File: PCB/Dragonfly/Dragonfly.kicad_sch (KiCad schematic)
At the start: 0 parts

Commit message: hell yeah
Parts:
- added U1: STM32F405RGTx, Package_QFP:LQFP-64_10x10mm_P0.5mm, symbol MCU_ST_STM32F4:STM32F405RGTx
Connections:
- new net: U1.18 (VSS), U1.63 (VSS)
- new net PA0: U1.14 (PA0)
- new net PA1: U1.15 (PA1)
- new net PA10: U1.43 (PA10)
- new net PA11: U1.44 (PA11)
- new net PA12: U1.45 (PA12)
- new net PA13: U1.46 (PA13)
- new net PA14: U1.49 (PA14)
- new net PA15: U1.50 (PA15)
- new net PA2: U1.16 (PA2)
- new net PA3: U1.17 (PA3)
- new net PA4: U1.20 (PA4)
- new net PA5: U1.21 (PA5)
- new net PA6: U1.22 (PA6)
- new net PA7: U1.23 (PA7)
- new net PA8: U1.41 (PA8)
- new net PA9: U1.42 (PA9)
- new net PB0: U1.26 (PB0)
- new net PB1: U1.27 (PB1)
- new net PB10: U1.29 (PB10)
- new net PB11: U1.30 (PB11)
- new net PB12: U1.33 (PB12)
- new net PB13: U1.34 (PB13)
- new net PB14: U1.35 (PB14)
- new net PB15: U1.36 (PB15)
- new net PB2: U1.28 (PB2)
- new net PB3: U1.55 (PB3)
- new net PB4: U1.56 (PB4)
- new net PB5: U1.57 (PB5)
- new net PB6: U1.58 (PB6)
- new net PB7: U1.59 (PB7)
- new net PB8: U1.61 (PB8)
- new net PB9: U1.62 (PB9)
- new net PC0: U1.8 (PC0)
- new net PC1: U1.9 (PC1)
- new net PC10: U1.51 (PC10)
- new net PC11: U1.52 (PC11)
- new net PC12: U1.53 (PC12)
- new net PC13: U1.2 (PC13)
- new net PC14: U1.3 (PC14)
- new net PC15: U1.4 (PC15)
- new net PC2: U1.10 (PC2)
- new net PC3: U1.11 (PC3)
- new net PC4: U1.24 (PC4)
- new net PC5: U1.25 (PC5)
- new net PC6: U1.37 (PC6)
- new net PC8: U1.38 (PC7)
- new net PC9: U1.39 (PC8)

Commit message: updated
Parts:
- added +10ppm: 32.768 kHz, symbol Device:Crystal
- added C1, C2: 100pf, symbol Device:C
- added C3, C4: 12pf, symbol Device:C
- added SW1: SW_SPDT_312, symbol Switch:SW_SPDT_312
- added X1: TSX-3225, TSX-3225, symbol TSX-3225:TSX-3225
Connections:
- net PC9 is gone; now on net PC8: U1.39 (PC8)
- net PC8: no longer U1.38 (PC7)
- net CP9: now reaches U1.40 (PC9)
- net at U1.5 (PH0): now also C1.2, X1.1
- net PD2: now reaches U1.54 (PD2)
- net at U1.6 (PH1): now also C2.2, X1.3
- net BOOT0: now reaches U1.60 (BOOT0)
- net NRST: now reaches U1.7 (NRST)
- net PA14: no longer names the net of U1.49 (PA14)
- net PA14: now also +10ppm.2, C3.1
- net PA15: no longer names the net of U1.50 (PA15)
- net PA15: now also +10ppm.1, C4.1
- new net: C2.1, X1.4
- new net: C1.1, X1.2
- new net GND: C3.2, C4.2
- new net PC7: U1.38 (PC7)
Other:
- note added: "MIAN MCU"
- moved on the sheet: U1

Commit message: updates
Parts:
- removed SW1: SW_SPDT_312, symbol Switch:SW_SPDT_312
- added C5: 100nf, symbol Device:C
- added R1: 10kΩ NC, symbol Device:R
- added R2, R3: 10kΩ, symbol Device:R
- added SW1, SW2: SW_SPST, symbol Switch:SW_SPST
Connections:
- net BOOT0: now also R2.2, SW2.1 (A)
- net GND: now also R2.1, R3.2
- net NRST: now also C5.1, R1.2, SW1.1 (A)
- net PB2: now also R3.1
- new net: C5.2, SW1.2 (B)
- new net VDD: R1.1, SW2.2 (B)
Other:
- note added: "BOOT Settings"
- note added: "Reset circuit"

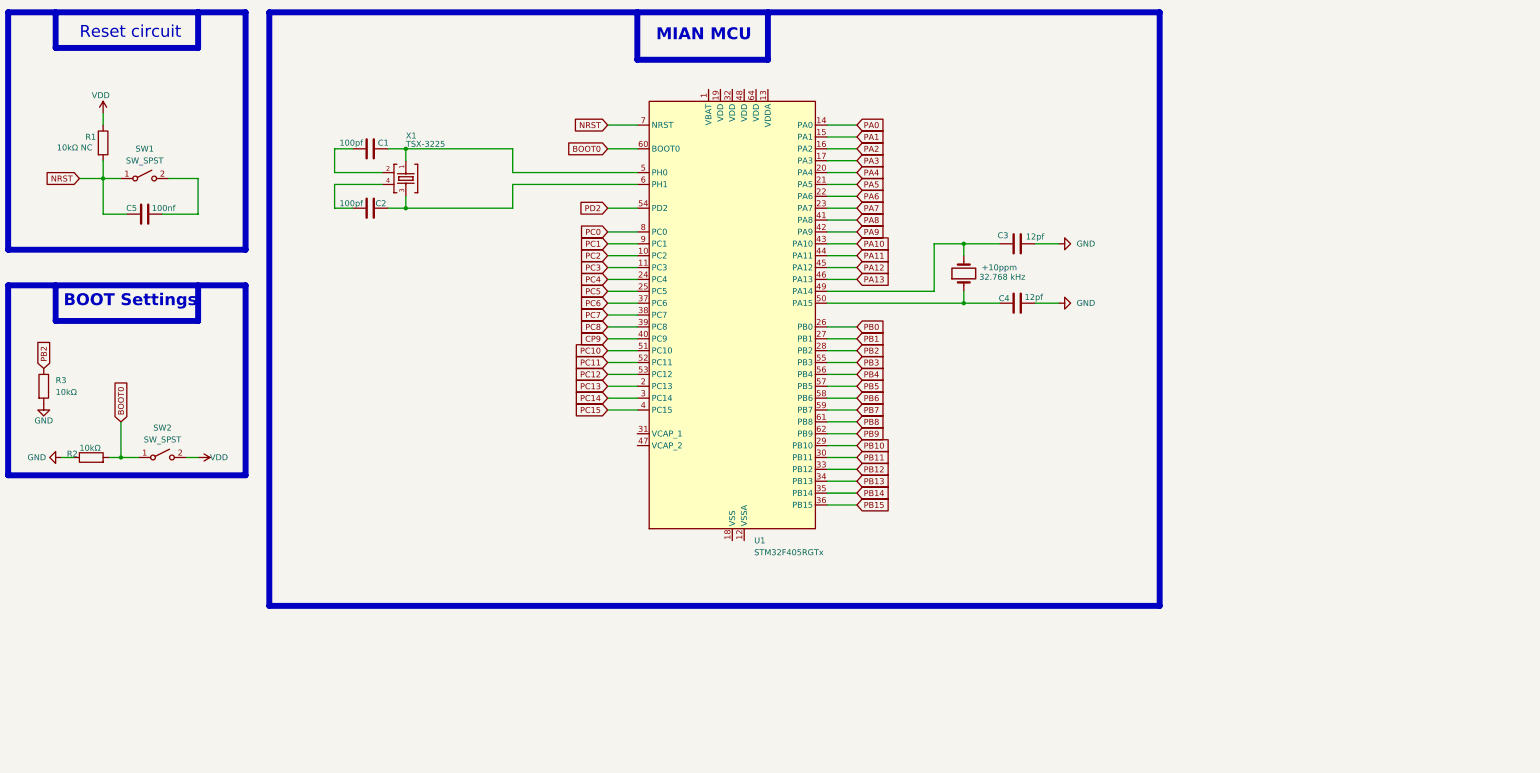
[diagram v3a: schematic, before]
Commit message: Update Dragonfly.kicad_sch
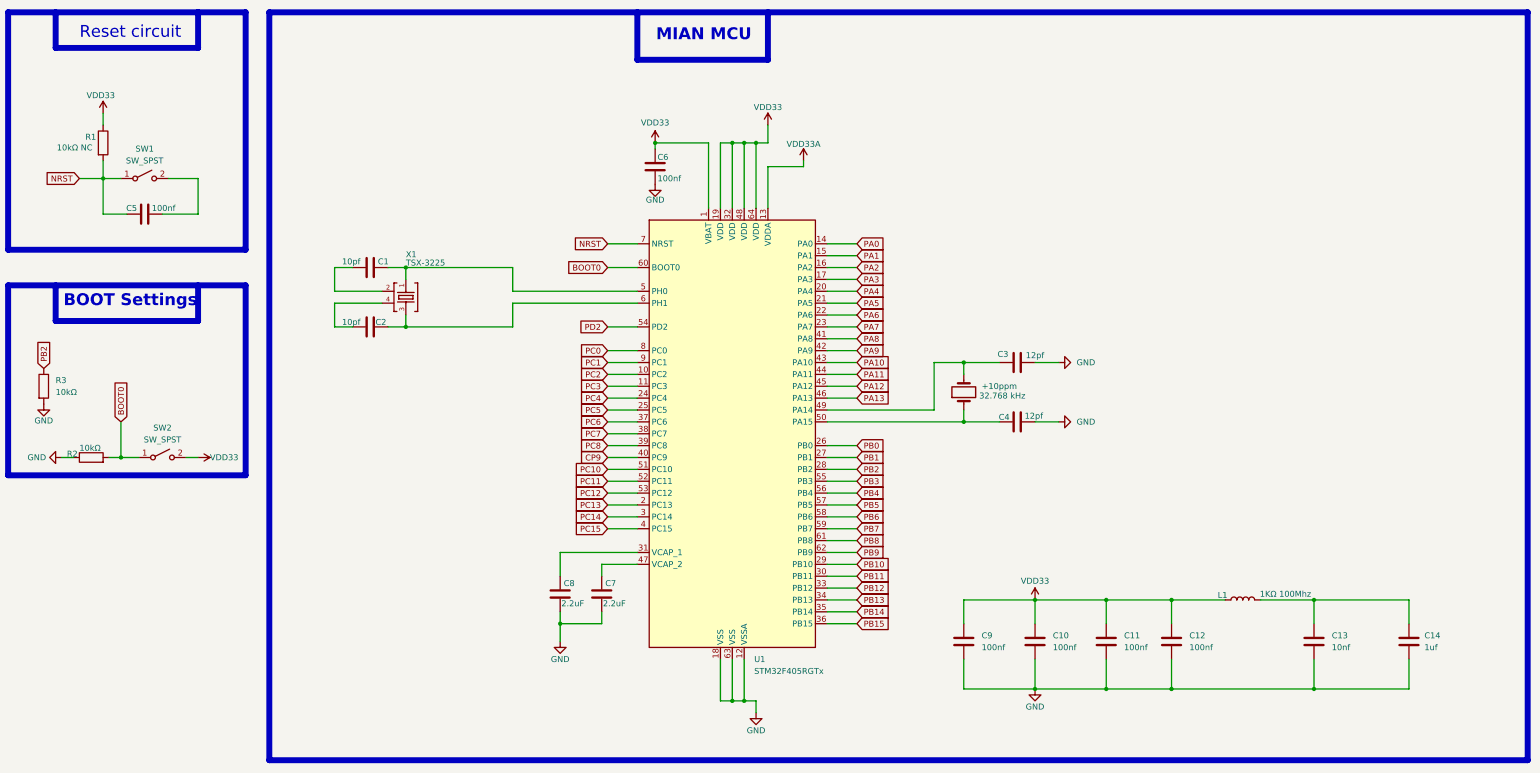
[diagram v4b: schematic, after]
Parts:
- added C10, C11, C12, C6, C9: 100nf, symbol Device:C
- added C13: 10nf, symbol Device:C
- added C14: 1uf, symbol Device:C
- added C7, C8: 2.2uF, symbol Device:C
- added L1: 1KΩ 100Mhz, symbol Device:L
- C1, C2: value 100pf -> 10pf
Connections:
- net VDD is gone; now on net VDD33: R1.1, SW2.2 (B)
- net GND: now also U1.12 (VSSA), U1.18 (VSS), U1.63 (VSS), C10.2, C11.2, C12.2, C13.2, C14.2, C6.2, C7.2, C8.2, C9.2
- net VDD33: now reaches U1.1 (VBAT)
- net VDD33: now also U1.19 (VDD), U1.32 (VDD), U1.48 (VDD), U1.64 (VDD), C10.1, C11.1, C12.1, C6.1, C9.1, L1.1
- net VDD33A: now reaches U1.13 (VDDA)
- net at U1.31 (VCAP_1): now also C8.1
- net at U1.47 (VCAP_2): now also C7.1
- new net: C13.1, C14.1, L1.2
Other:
- moved on the sheet: +10ppm, C1, C2, C3, C4, X1

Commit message: Update Dragonfly.kicad_sch
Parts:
- removed +10ppm: 32.768 kHz, symbol Device:Crystal
- added +10ppm1: 32.768 kHz, symbol Device:Crystal
- added C15, C19: 100nf, symbol Device:C
- added C16: 4.7uF, symbol Device:C
- added C17, C18: 10uf, symbol Device:C
- added D1: blue, symbol Device:D
- added D2: red, symbol Device:D
- added D3: DSK 34 SOD123, symbol Device:D
- added J1: Conn_01x04_Pin, symbol Connector:Conn_01x04_Pin
- added J2: Micro_SD_Card, symbol Connector:Micro_SD_Card
- added J3: USB_C_Receptacle_USB2.0_16P, symbol Connector:USB_C_Receptacle_USB2.0_16P
- added JP1: SolderJumper_2_Bridged, symbol Jumper:SolderJumper_2_Bridged
- added R4, R5, R7, R8: 5.1kΩ, symbol Device:R
- added R6: R, symbol Device:R
- added U2: (no value), Package_TO_SOT_SMD:SOT-89-3, symbol ME6231A33PG:ME6231A33PG
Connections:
- net PC14 is gone; now on an unnamed net: U1.3 (PC14)
- net PC15 is gone; now on an unnamed net: U1.4 (PC15)
- net CP9: now also J2.8 (DAT1)
- net GND: now also C15.2, C16.2, C17.2, C18.2, C19.2, D1.2 (A), D2.2 (A), J1.3 (Pin_3), J2.6 (VSS), J2.SH (SHIELD), J3.A1 (GND), J3.A12 (GND), J3.A8 (SBU1), J3.B1 (GND), J3.B12 (GND), J3.B8 (SBU2), J3.SH (SHIELD), R7.2, R8.2, U2.3 (VOUT)
- net PA11: now also J3.A6 (D+)
- net PA12: now also J3.B6 (D+)
- net PA13: now also J1.2 (Pin_2)
- net PB2: now also R4.1
- net PC10: now also J2.1 (DAT2)
- net PC11: now also J2.2 (DAT3/CD), R6.2
- net PC12: now also J2.5 (CLK)
- net PC8: now also J2.7 (DAT0)
- net PD2: now also J2.3 (CMD)
- net VDD33: now also C15.1, C16.1, C17.1, J1.1 (Pin_1), J2.4 (VDD), R5.1, R6.1, U2.1 (GND)
- net VDD33A: now also C13.1, C14.1, L1.2
- net at C4.1: now also +10ppm1.1; no longer U1.50 (PA15)
- net at C3.1: now also +10ppm1.2; no longer U1.49 (PA14)
- new net: D1.1 (K), R4.2
- new net: D2.1 (K), R5.2
- new net CC1: J3.A5 (CC1), R7.1
- new net CC2: J3.B5 (CC2), R8.1
- new net PA14: J1.4 (Pin_4), U1.49 (PA14)
- new net PA15: U1.50 (PA15)
- new net VBUS: C19.1, D3.1 (K), J3.A4 (VBUS), J3.A9 (VBUS), J3.B4 (VBUS), J3.B9 (VBUS), JP1.1 (A)
- new net VCC: C18.1, D3.2 (A), JP1.2 (B), U2.2 (VIN)
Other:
- note added: "Indicator light"
- note added: "SW debug download interface"
- note added: "TF interface"
- note added: "USB-C 16 PIN"
- note added: "VCC -> 3.3V Power conversion"

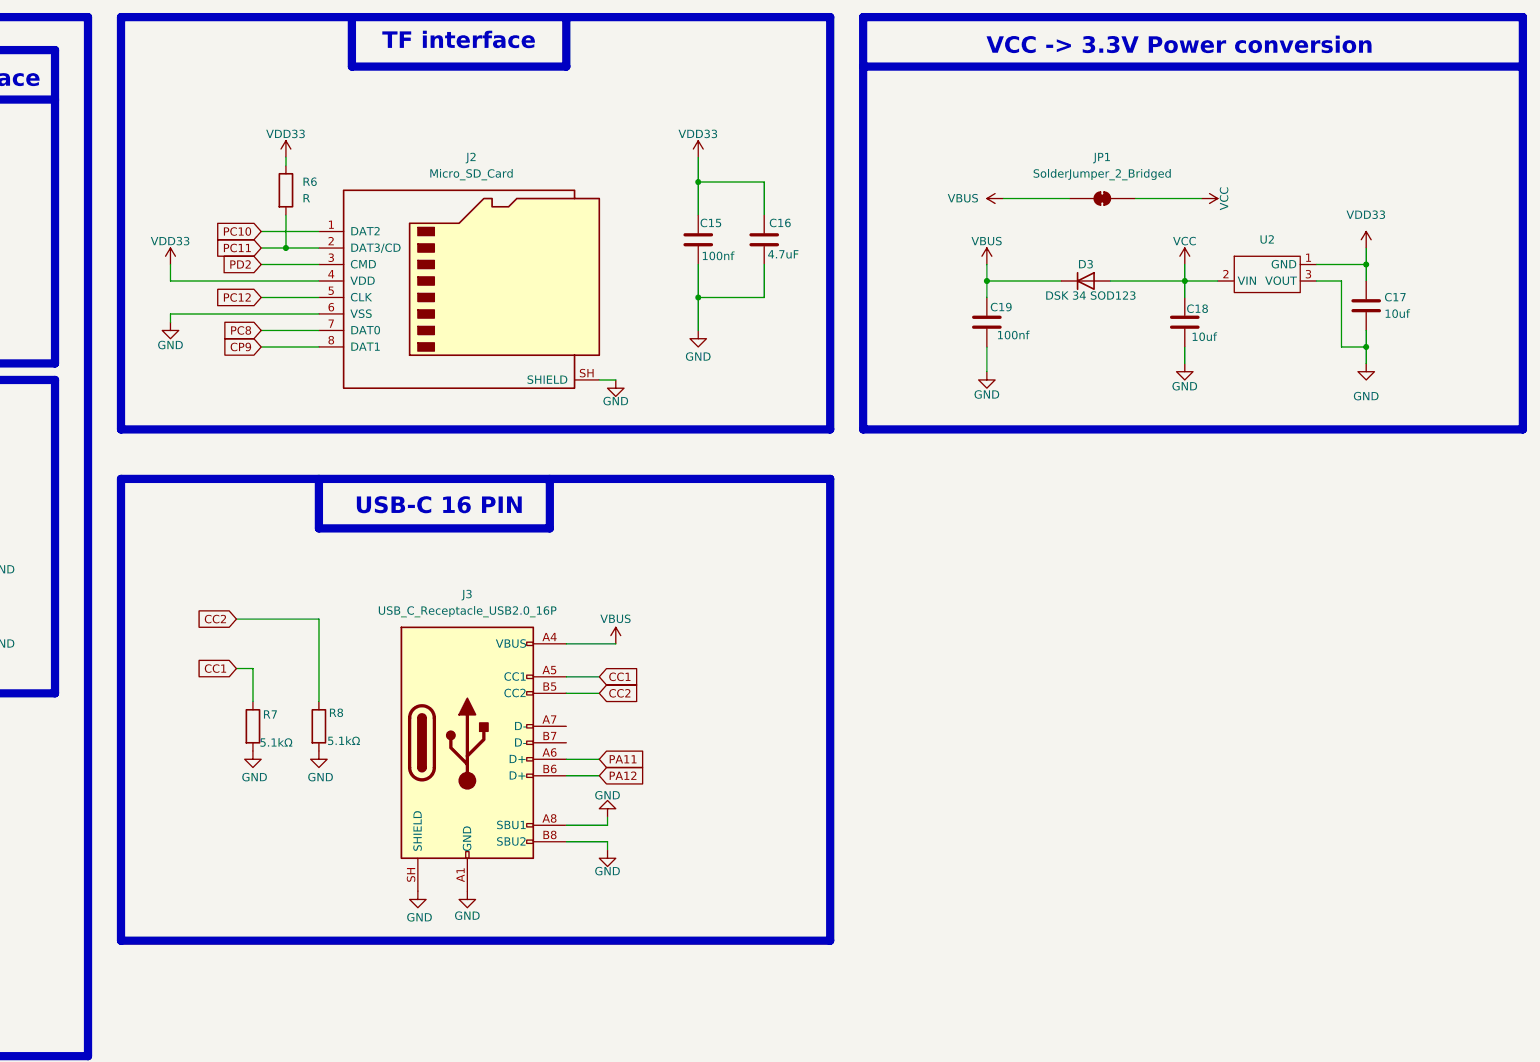
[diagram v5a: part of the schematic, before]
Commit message: Update Dragonfly.kicad_sch
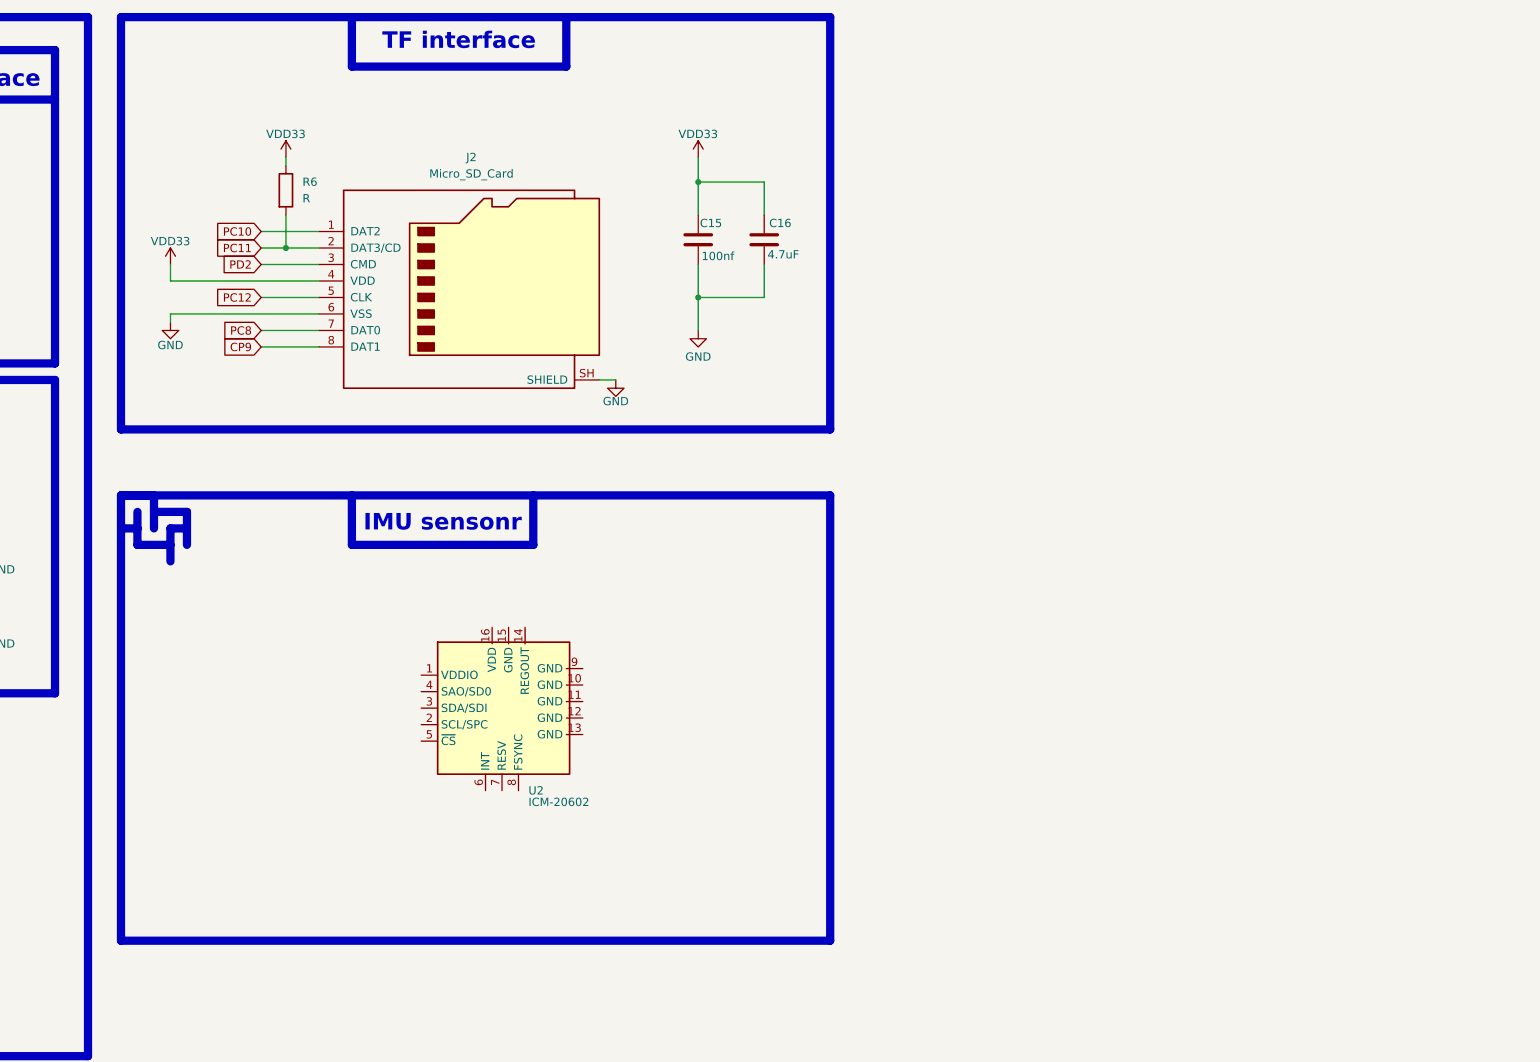
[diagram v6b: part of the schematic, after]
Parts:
- removed C17, C18: 10uf, symbol Device:C
- removed C19: 100nf, symbol Device:C
- removed D3: DSK 34 SOD123, symbol Device:D
- removed J3: USB_C_Receptacle_USB2.0_16P, symbol Connector:USB_C_Receptacle_USB2.0_16P
- removed JP1: SolderJumper_2_Bridged, symbol Jumper:SolderJumper_2_Bridged
- removed R7, R8: 5.1kΩ, symbol Device:R
- removed U2: (no value), Package_TO_SOT_SMD:SOT-89-3, symbol ME6231A33PG:ME6231A33PG
- added U2: ICM-20602, Package_LGA:LGA-16_3x3mm_P0.5mm_LayoutBorder3x5y, symbol Sensor_Motion:ICM-20602
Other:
- note added: "IMU sensonr"
- note removed: "USB-C 16 PIN"
- note removed: "VCC -> 3.3V Power conversion"

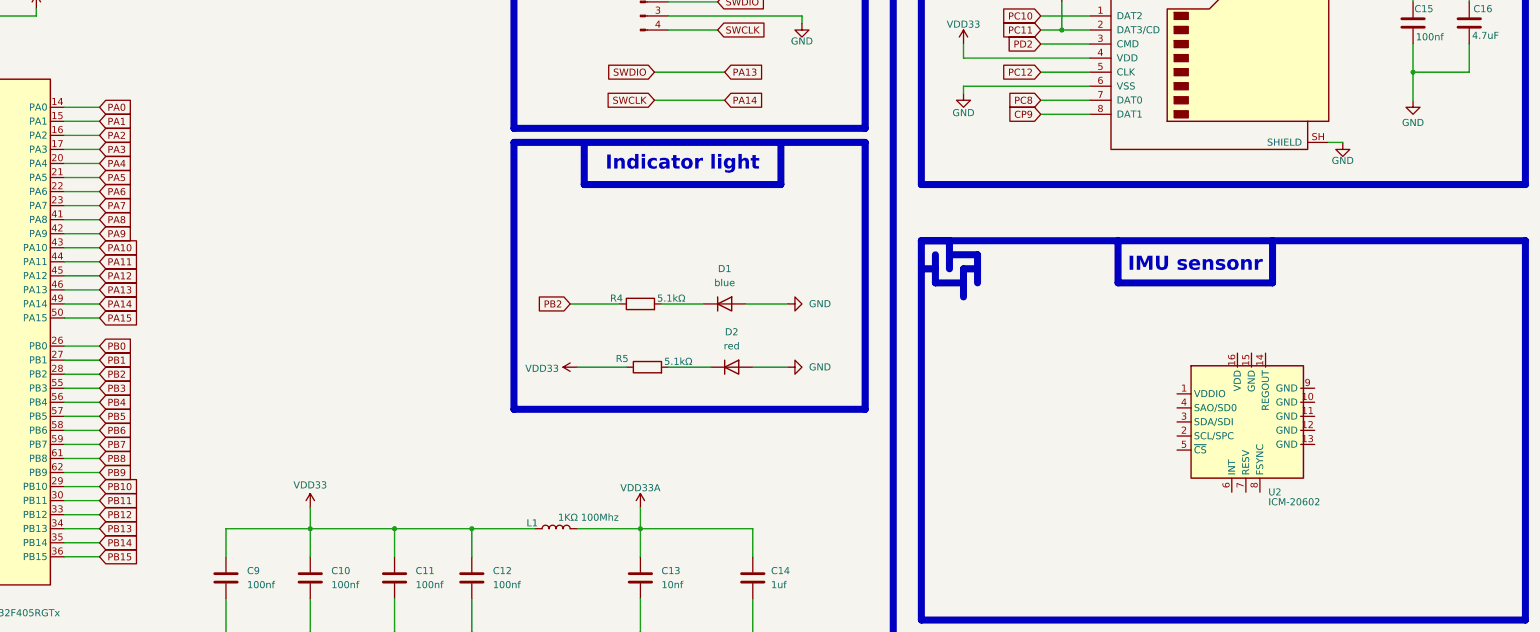
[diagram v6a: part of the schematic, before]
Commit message: Update Dragonfly.kicad_sch
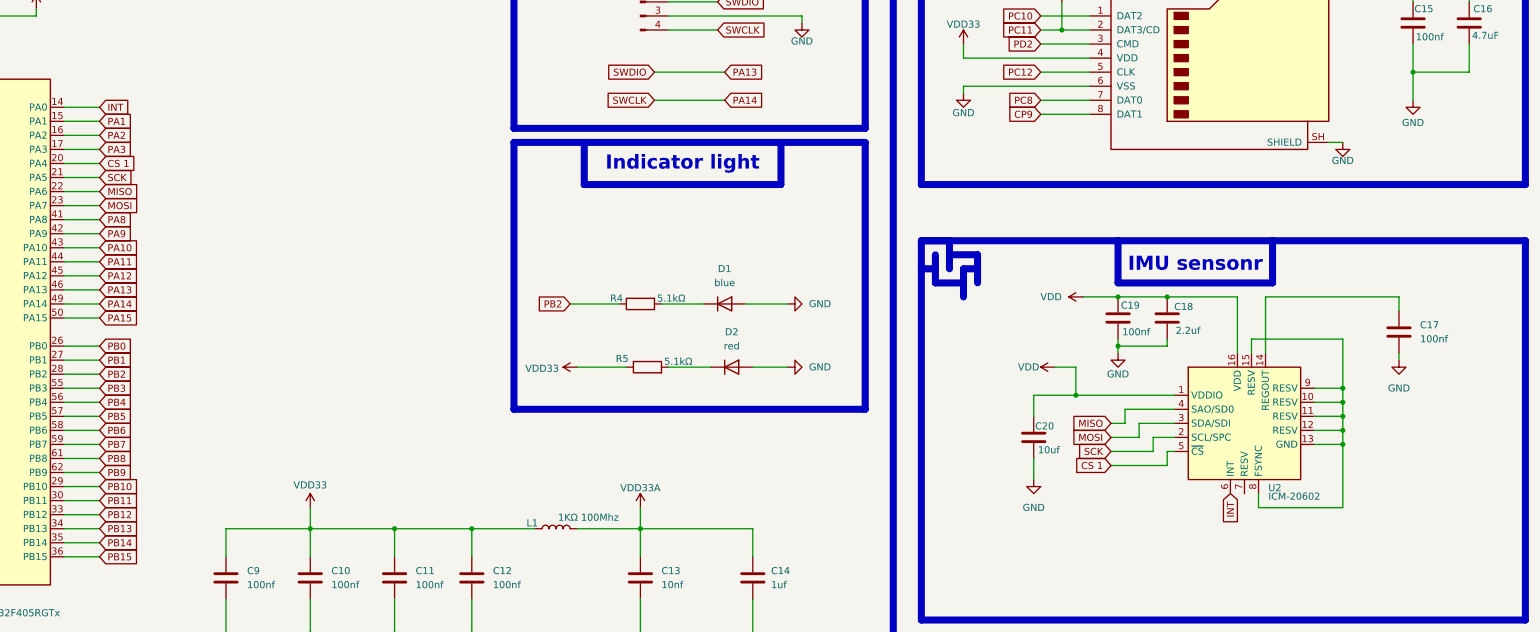
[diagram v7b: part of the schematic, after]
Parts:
- added C17, C19: 100nf, symbol Device:C
- added C18: 2.2uf, symbol Device:C
- added C20: 10uf, symbol Device:C
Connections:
- net PA0 is gone; now on net INT: U1.14 (PA0)
- net PA4 is gone; now on net CS 1: U1.20 (PA4)
- net PA5 is gone; now on net SCK: U1.21 (PA5)
- net PA6 is gone; now on net MISO: U1.22 (PA6)
- net PA7 is gone; now on net MOSI: U1.23 (PA7)
- net GND: now also C17.2, C18.2, C19.2, C20.2
- net VDD: now reaches U2.1 (VDDIO)
- net VDD: now also U2.16 (VDD), C18.1, C19.1, C20.1
- net at U2.10 (RESV): now also U2.11 (RESV), U2.12 (RESV), U2.13 (GND), U2.15 (RESV), U2.8 (FSYNC), U2.9 (RESV)
- net at U2.14 (REGOUT): now also C17.1
- net SCK: now reaches U2.2 (SCL/SPC)
- net MOSI: now reaches U2.3 (SDA/SDI)
- net MISO: now reaches U2.4 (SAO/SD0)
- net CS 1: now reaches U2.5 (~{CS})
- net INT: now reaches U2.6 (INT)
